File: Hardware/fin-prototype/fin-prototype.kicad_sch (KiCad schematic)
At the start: 80 parts, among them J1 USB_C_Receptacle_USB2.0_16P, J10 Conn_01x01_Pin, J11 Conn_01x01_Pin, J12 Conn_01x01_Pin, J13 Conn_01x01_Pin, J14 Conn_01x01_Pin, J15 Conn_01x01_Pin, J16 Conn_01x01_Pin, J17 Conn_01x01_Pin, J18 Conn_01x01_Pin, J2 Conn_01x04_Pin, J3 Conn_01x04_Pin, J4 Conn_01x08_Pin, J5 Conn_01x04_Pin, J6 Conn_01x01_Pin, J7 Conn_01x01_Pin, J8 Conn_01x01_Pin, J9 Conn_01x01_Pin, SW1 SW_Push, SW2 SW_Push, U1 ADS131M03QPWRQ1, U2 STM32L412C8Tx, U3 W25N512GVEIG, U4 TMP235A4DBZR, U5 FT232RNQ-REEL

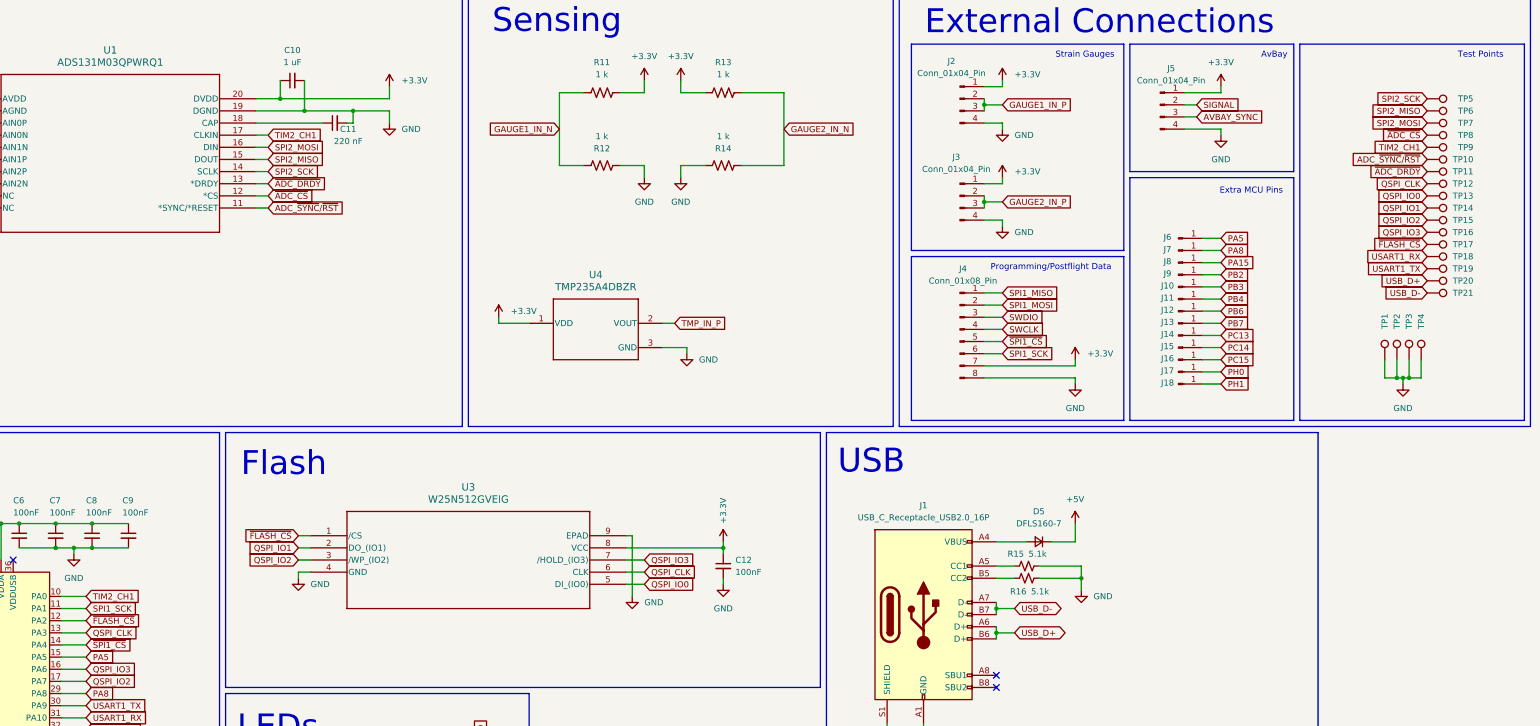
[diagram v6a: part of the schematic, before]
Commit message: finish up silkscreen
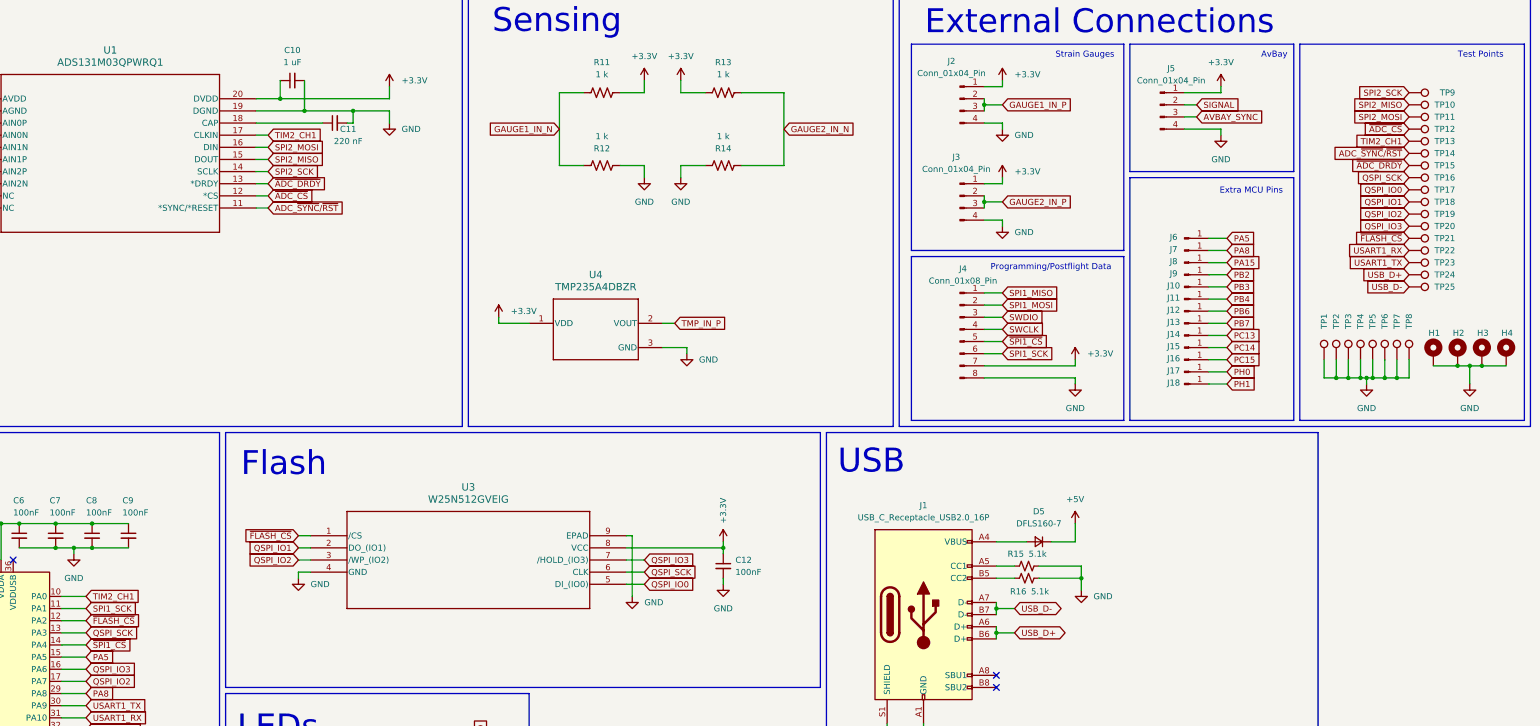
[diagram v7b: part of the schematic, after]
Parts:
- added H1, H2, H3, H4: MountingHole_Pad, MountingHole:MountingHole_2.2mm_M2_Pad, symbol Mechanical:MountingHole_Pad
- added TP5, TP6, TP7, TP8: TestPoint, Connector_PinSocket_2.54mm:PinSocket_1x01_P2.54mm_Vertical, symbol Connector:TestPoint
- D1: Signal (none) -> PWR
- D2: Signal (none) -> TX
- D3: Signal (none) -> RX
- D4: Signal (none) -> STATUS
- J10: footprint Connector_PinHeader_2.54mm:PinHeader_1x01_P2.54mm_Vertical -> FinLib:SimpleThroughHole; MCU Pin (none) -> PB3
- J11: footprint Connector_PinHeader_2.54mm:PinHeader_1x01_P2.54mm_Vertical -> FinLib:SimpleThroughHole; MCU Pin (none) -> PB4
- J12: footprint Connector_PinHeader_2.54mm:PinHeader_1x01_P2.54mm_Vertical -> FinLib:SimpleThroughHole; MCU Pin (none) -> PB6
- J13: footprint Connector_PinHeader_2.54mm:PinHeader_1x01_P2.54mm_Vertical -> FinLib:SimpleThroughHole; MCU Pin (none) -> PB7
- J14: footprint Connector_PinHeader_2.54mm:PinHeader_1x01_P2.54mm_Vertical -> FinLib:SimpleThroughHole; MCU Pin (none) -> PC13
- J15: footprint Connector_PinHeader_2.54mm:PinHeader_1x01_P2.54mm_Vertical -> FinLib:SimpleThroughHole; MCU Pin (none) -> PC14
- J16: footprint Connector_PinHeader_2.54mm:PinHeader_1x01_P2.54mm_Vertical -> FinLib:SimpleThroughHole; MCU Pin (none) -> PC15
- J17: footprint Connector_PinHeader_2.54mm:PinHeader_1x01_P2.54mm_Vertical -> FinLib:SimpleThroughHole; MCU Pin (none) -> PH0
- J18: footprint Connector_PinHeader_2.54mm:PinHeader_1x01_P2.54mm_Vertical -> FinLib:SimpleThroughHole; MCU Pin (none) -> PH1
- J6: footprint Connector_PinHeader_2.54mm:PinHeader_1x01_P2.54mm_Vertical -> FinLib:SimpleThroughHole; MCU Pin (none) -> PA5
- J7: footprint Connector_PinHeader_2.54mm:PinHeader_1x01_P2.54mm_Vertical -> FinLib:SimpleThroughHole; MCU Pin (none) -> PA8
- J8: footprint Connector_PinHeader_2.54mm:PinHeader_1x01_P2.54mm_Vertical -> FinLib:SimpleThroughHole; MCU Pin (none) -> PA15
- J9: footprint Connector_PinHeader_2.54mm:PinHeader_1x01_P2.54mm_Vertical -> FinLib:SimpleThroughHole; MCU Pin (none) -> PB2
- SW1: Function (none) -> RST
- SW2: Function (none) -> BOOT
- TP1, TP2, TP3, TP4: footprint TestPoint:TestPoint_Loop_D1.80mm_Drill1.0mm_Beaded -> Connector_PinHeader_2.54mm:PinHeader_1x01_P2.54mm_Vertical
- TP10: renamed from TP6; Signal (none) -> MISO
- TP11: renamed from TP7; Signal (none) -> MOSI
- TP12: renamed from TP8; Signal (none) -> CS
- TP13: renamed from TP9; Signal (none) -> CLK
- TP14: renamed from TP10; Signal (none) -> RST
- TP15: renamed from TP11; Signal (none) -> DRDY
- TP16: renamed from TP12; Signal (none) -> SCK
- TP17: renamed from TP13; Signal (none) -> IO0
- TP18: renamed from TP14; Signal (none) -> IO1
- TP19: renamed from TP15; Signal (none) -> IO2
- TP20: renamed from TP16; Signal (none) -> IO3
- TP22: renamed from TP18; Signal (none) -> RX
- TP23: renamed from TP19; Signal (none) -> TX
- TP24: renamed from TP20; Signal (none) -> USB+
- TP25: renamed from TP21; Signal (none) -> USB-
- TP9: renamed from TP5; Signal (none) -> SCK
- renumbered TP17 to TP21
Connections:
- net GND: now also H1.1, H2.1, H3.1, H4.1, TP5.1, TP6.1, TP7.1, TP8.1
- net QSPI_CLK renamed QSPI_SCK
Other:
- moved on the sheet: J10, J11, J12, J13, J14, J15, J16, J17, J18, J6, J7, J8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
